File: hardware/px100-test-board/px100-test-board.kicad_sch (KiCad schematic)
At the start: 0 parts

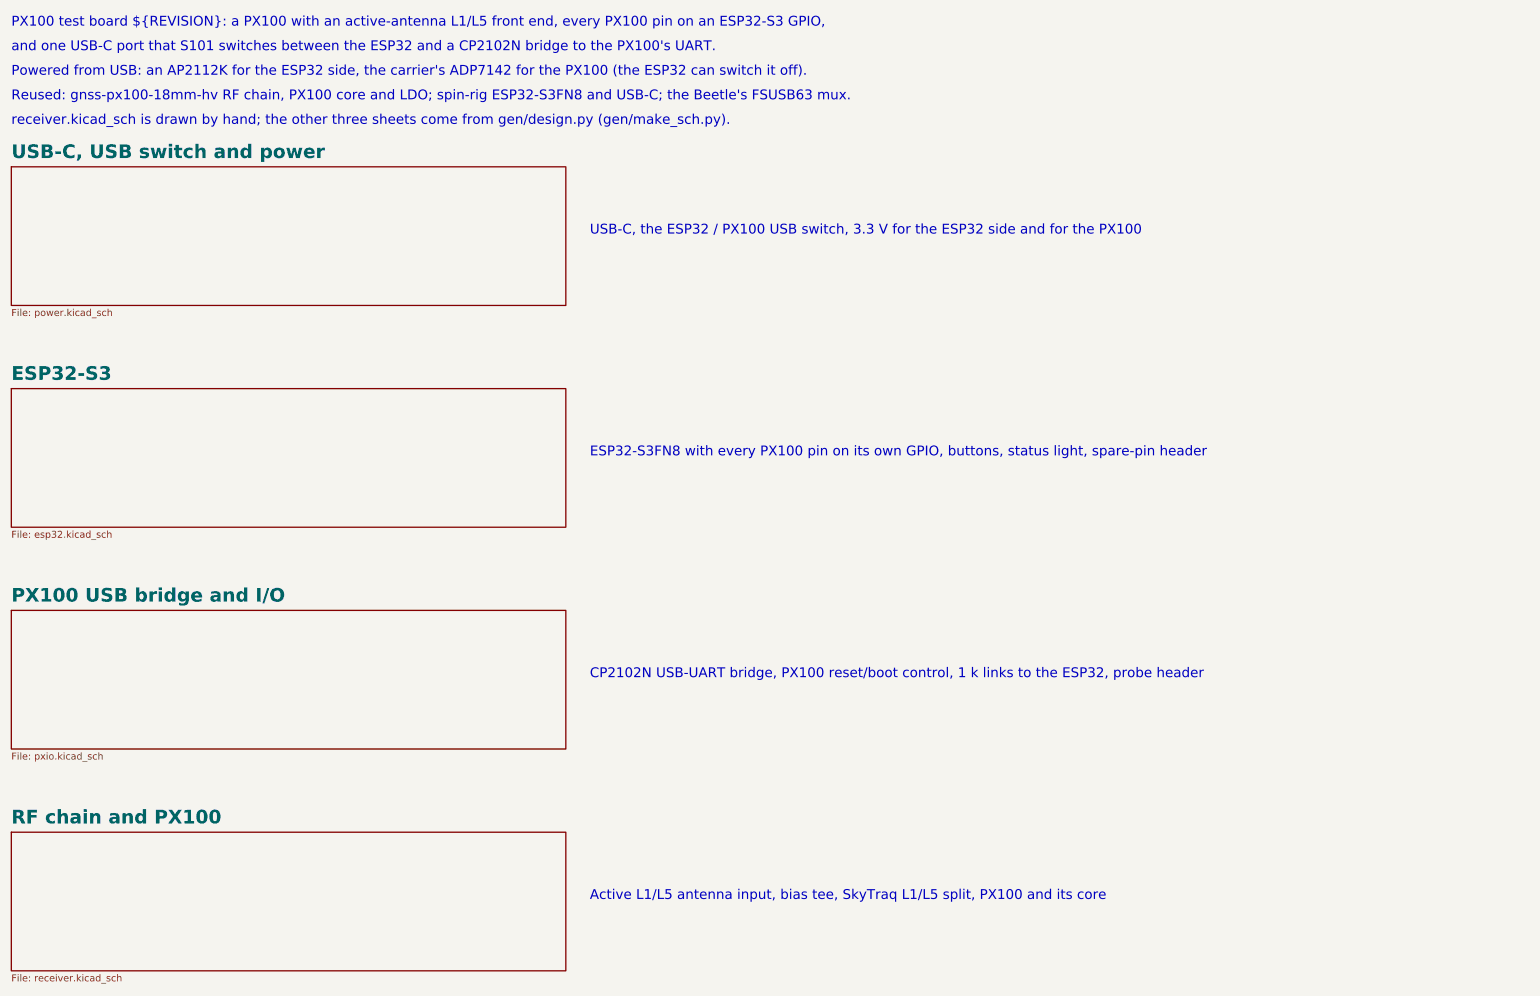
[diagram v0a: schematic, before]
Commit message: hardware(px100-test-board): ESP32-S3FH4R2 in place of the FN8 -- the Beetle JLC build's part
Same QFN-56 footprint and pinout, so the layout is untouched: only U201's
value, MPN and LCSC fields change (C3013940, 2,862 at JLC on 2026-10-29).
The FH4R2 has 4 MB of flash and 2 MB of quad PSRAM in the package; its
flash pins (GPIO27-32) and the PSRAM's chip select (SPICS1/GPIO26) were
already unconnected here, and quad PSRAM leaves GPIO33-37 free for J201 and
USB_SEL_MCU. Firmware needs a 4 MB flash size and partition table.

ERC 0 errors; DRC 0 errors, 0 unconnected, schematic parity 0;
tools/check_board_parity.py passes.

Co-Authored-By: Claude Opus 5.5 <noreply@anthropic.com>
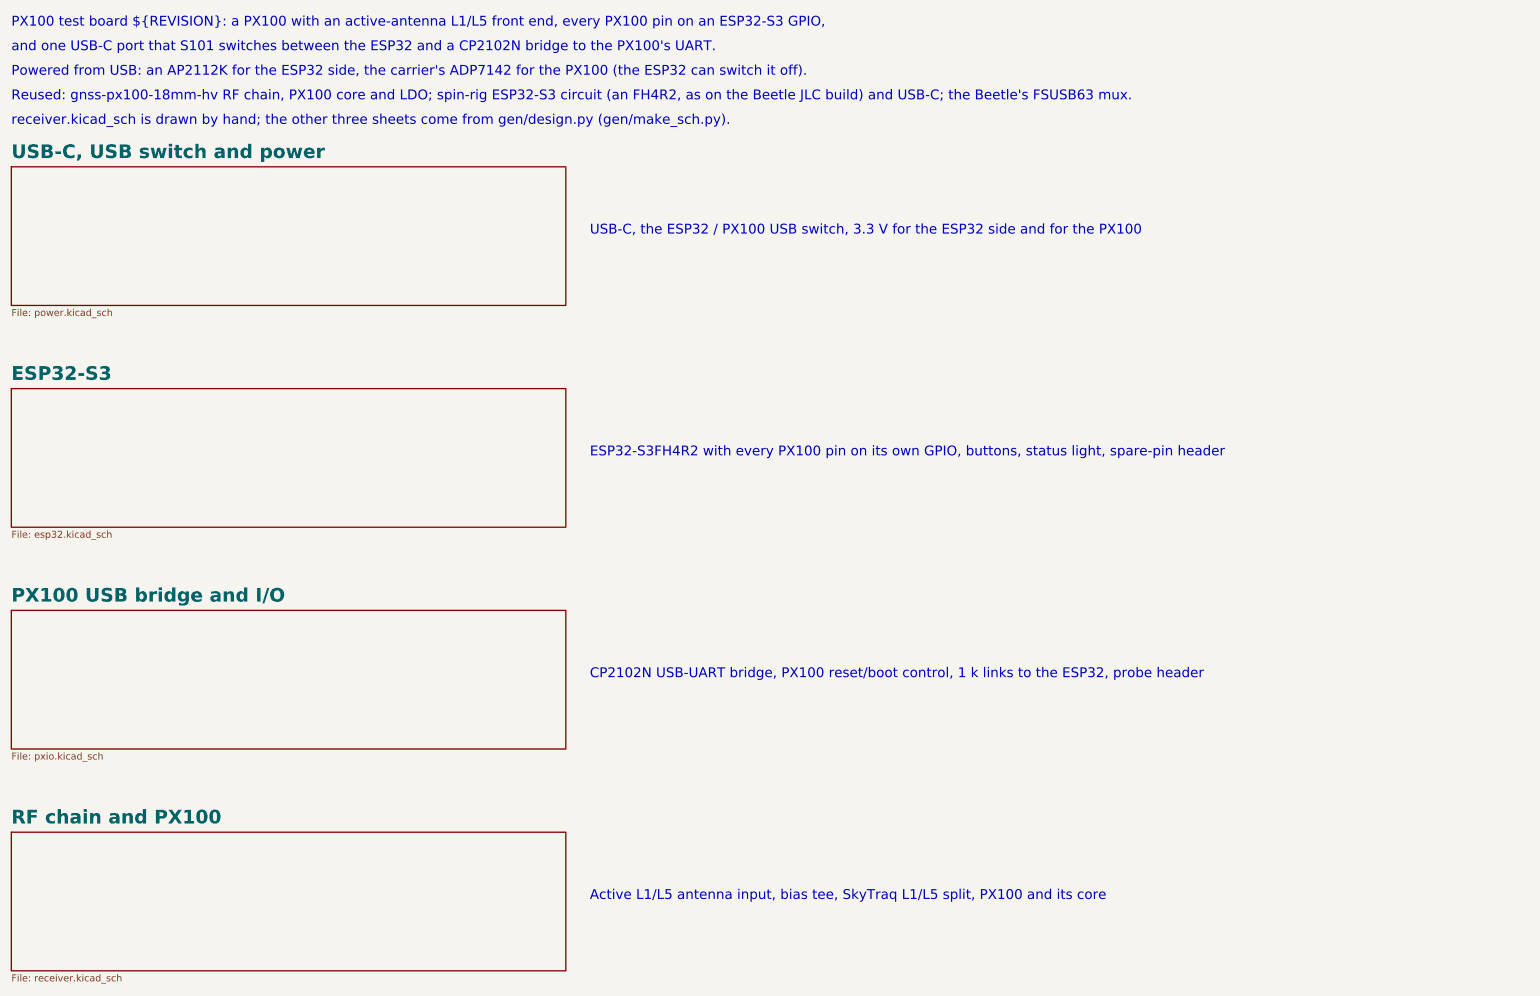
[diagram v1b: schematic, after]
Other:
- note added: "ESP32-S3FH4R2 with every PX100 pin on its own GPIO, buttons, status light, spare-pin header"
- note added: "Reused: gnss-px100-18mm-hv RF chain, PX100 core and LDO; spin-rig ESP32-S3 circuit (an FH4R2, as on the Beetle JLC build) and USB-C; the Beetle's FSUSB63 mux."
- note removed: "ESP32-S3FN8 with every PX100 pin on its own GPIO, buttons, status light, spare-pin header"
- note removed: "Reused: gnss-px100-18mm-hv RF chain, PX100 core and LDO; spin-rig ESP32-S3FN8 and USB-C; the Beetle's FSUSB63 mux."
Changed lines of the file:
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@@
 		)
 	)
-	(text "ESP32-S3FN8 with every PX100 pin on its own GPIO, buttons, status light, spare-pin header"
+	(text "ESP32-S3FH4R2 with every PX100 pin on its own GPIO, buttons, status light, spare-pin header"
 		(exclude_from_sim no)
 		(at 131.4 104.14 0)
@@
 		)
 	)
-	(text "Reused: gnss-px100-18mm-hv RF chain, PX100 core and LDO; spin-rig ESP32-S3FN8 and USB-C; the Beetle's FSUSB63 mux."
+	(text "Reused: gnss-px100-18mm-hv RF chain, PX100 core and LDO; spin-rig ESP32-S3 circuit (an FH4R2, as on the Beetle JLC build) and USB-C; the Beetle's FSUSB63 mux."
 		(exclude_from_sim no)
 		(at 25.4 38.9 0)
